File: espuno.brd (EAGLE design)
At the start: 68.6 x 53.3 mm, 62 parts, among them J1 ARDUINO_R3_SHIELD, T1 FDN340P, U1 ADS1115IDGST, U2 NCP1117ST50T3G, U3 LP2985-33DBVR, U4 FT232R, U5 LMV358IDGKR, U6 MCP73831, U7 TPS61200, X1 POWERSUPPLY_DC21MMX

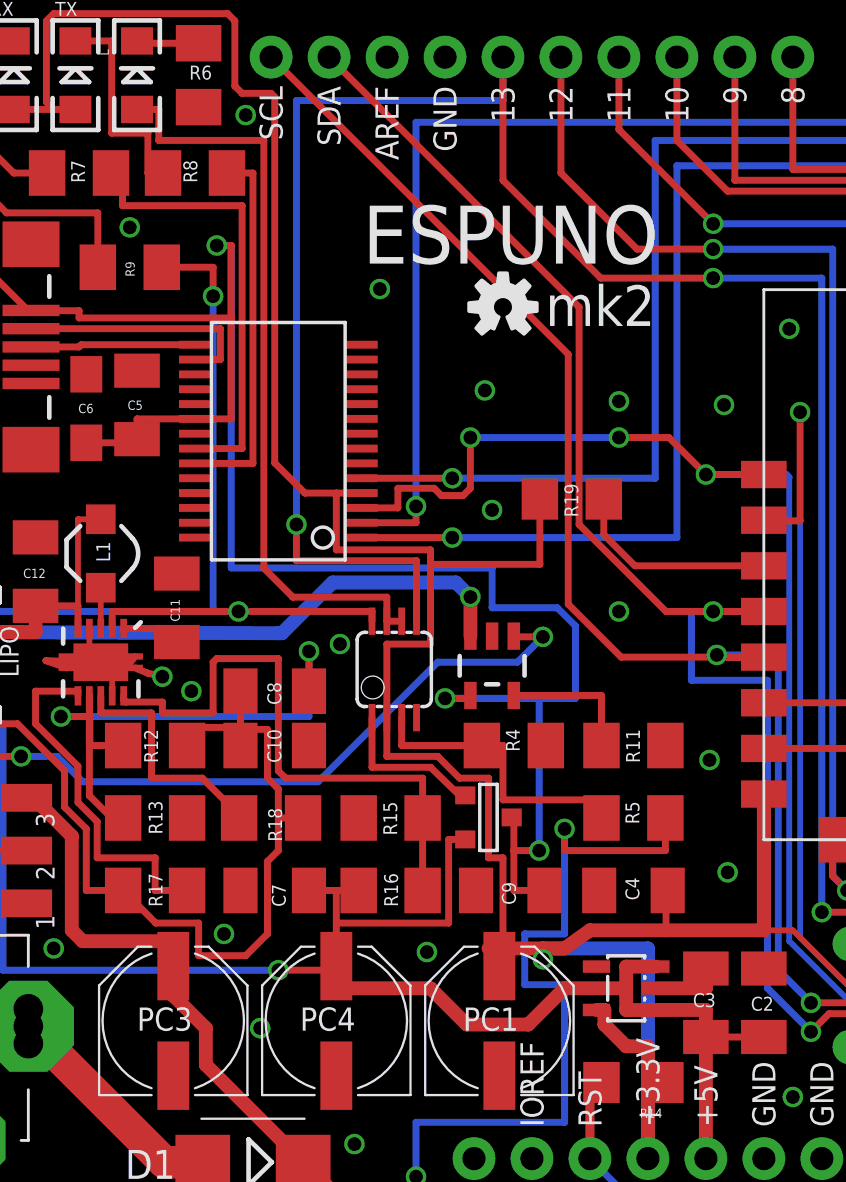
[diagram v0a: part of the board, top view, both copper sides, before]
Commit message: Fix bug with TX/RX switched, renumber PC1,PC3,PC4 to be PC1-3 in order of decreasing voltage rail.
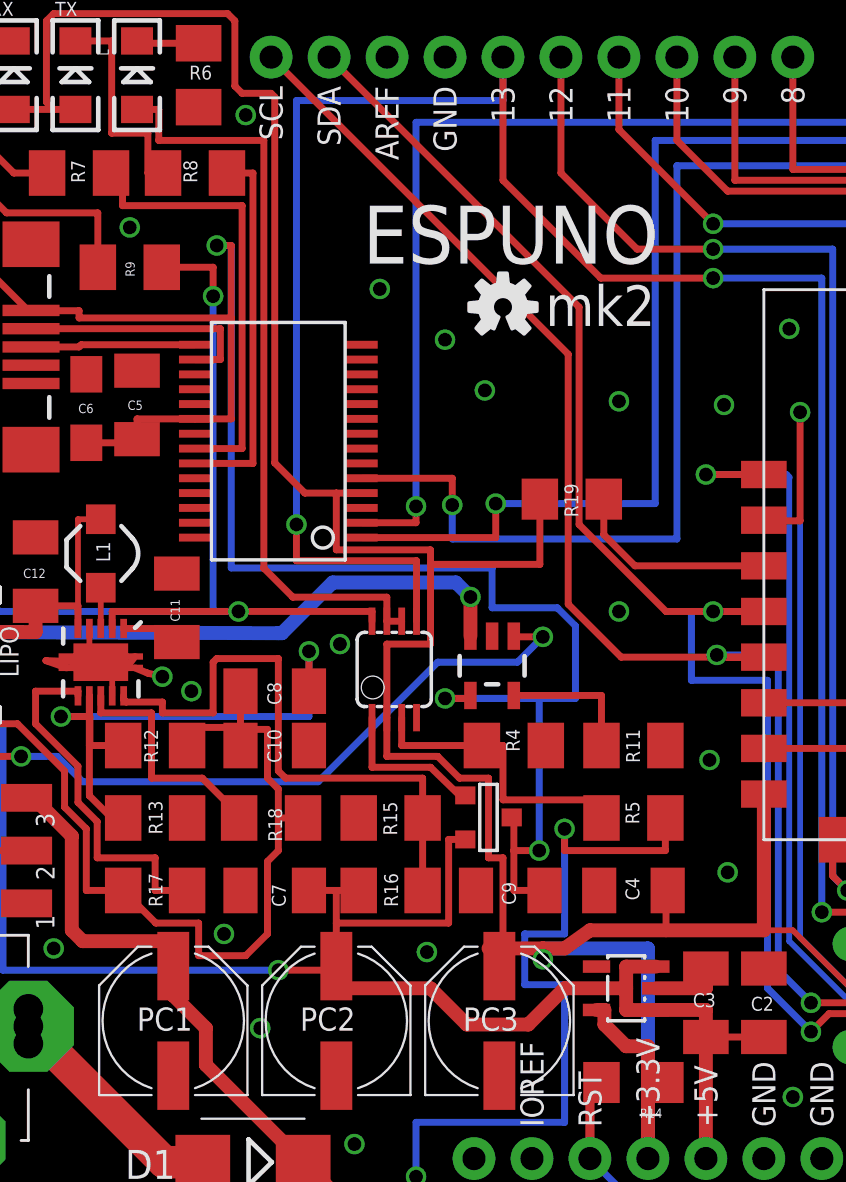
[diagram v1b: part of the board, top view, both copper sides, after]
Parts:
- moved PC1 14.3 mm to (14.8, 8.57)
- moved PC3 14.3 mm to (29.1, 8.57)
- renumbered PC4 to PC2
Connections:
- net 3.3V: now also PC3.+; no longer PC1.+
- net RESET: no longer U4.3
- net RX: now also U4.1; no longer U4.5
- net TX: now also U4.5; no longer U4.1
- net VIN: now also PC1.+; no longer PC3.+
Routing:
- net RESET: track 126.2 -> 107.1 mm, vias 3 -> 1
- net TX: track 79.4 -> 82.1 mm
- net RX: track 85.9 -> 88.5 mm
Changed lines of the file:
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@@
 <?xml version="1.0" encoding="utf-8"?>
 <!DOCTYPE eagle SYSTEM "eagle.dtd">
-<eagle version="7.2.0">
+<eagle version="7.4.0">
 <drawing>
 <settings>
@@
 <grid distance="0.00625" unitdist="inch" unit="inch" style="lines" multiple="1" display="no" altdistance="0.00625" altunitdist="inch" altunit="inch"/>
 <layers>
-<layer number="1" name="Top" color="4" fill="1" visible="no" active="yes"/>
-<layer number="16" name="Bottom" color="1" fill="1" visible="no" active="yes"/>
+<layer number="1" name="Top" color="4" fill="1" visible="yes" active="yes"/>
+<layer number="16" name="Bottom" color="1" fill="1" visible="yes" active="yes"/>
 <layer number="17" name="Pads" color="2" fill="1" visible="yes" active="yes"/>
 <layer number="18" name="Vias" color="2" fill="1" visible="yes" active="yes"/>
@@
 <element name="JP1" library="SparkFun-Connectors" package="USB-MINIB-NOSTOP" value="USB-SMD-NS" x="6.0325" y="38.1" smashed="yes"/>
 <element name="J1" library="SparkFun-Boards" package="UNO_R3_SHIELD" value="ARDUINO_R3_SHIELD" x="8.89" y="53.34" smashed="yes" rot="R270"/>
-<element name="PC3" library="rcl" package="PANASONIC_D" value="47u" x="14.76375" y="8.5725" smashed="yes" rot="R90">
+<element name="PC1" library="rcl" package="PANASONIC_D" value="47u" x="14.76375" y="8.5725" smashed="yes" rot="R90">
 <attribute name="NAME" x="13.1725" y="8.14375" size="1.016" layer="25"/>
 </element>
-<element name="PC4" library="rcl" package="PANASONIC_D" value="47u" x="21.9075" y="8.5725" smashed="yes" rot="R90">
+<element name="PC2" library="rcl" package="PANASONIC_D" value="47u" x="21.9075" y="8.5725" smashed="yes" rot="R90">
 <attribute name="NAME" x="20.31625" y="8.14375" size="1.016" layer="25"/>
 </element>
-<element name="PC1" library="rcl" package="PANASONIC_D" value="47u" x="29.05125" y="8.5725" smashed="yes" rot="R90">
+<element name="PC3" library="rcl" package="PANASONIC_D" value="47u" x="29.05125" y="8.5725" smashed="yes" rot="R90">
 <attribute name="NAME" x="27.46" y="8.14375" size="1.016" layer="25"/>
 </element>
@@
 <signal name="RX">
 <contactref element="MDL1" pad="15"/>
-<contactref element="U4" pad="5"/>
 <contactref element="J1" pad="RX"/>
 <wire x1="56.84" y1="30.51" x2="61.43625" y2="30.51" width="0.3048" layer="1"/>
@@
 <wire x1="61.43625" y1="48.895" x2="63.5" y2="48.895" width="0.3048" layer="1"/>
 <wire x1="63.5" y1="48.895" x2="63.5" y2="50.8" width="0.3048" layer="1"/>
-<wire x1="23.0235" y1="32.3475" x2="26.9875" y2="32.3475" width="0.3048" layer="1"/>
-<via x="26.9875" y="32.3475" extent="1-16" drill="0.6"/>
-<wire x1="26.9875" y1="32.3475" x2="35.8775" y2="32.3475" width="0.3048" layer="16"/>
-<wire x1="35.8775" y1="32.3475" x2="35.8775" y2="47.14875" width="0.3048" layer="16"/>
+<via x="28.8925" y="31.23625" extent="1-16" drill="0.6"/>
+<wire x1="28.8925" y1="31.23625" x2="35.8775" y2="31.23625" width="0.3048" layer="16"/>
+<wire x1="35.8775" y1="31.23625" x2="35.8775" y2="47.14875" width="0.3048" layer="16"/>
 <wire x1="35.8775" y1="47.14875" x2="63.5" y2="47.14875" width="0.3048" layer="16"/>
 <wire x1="63.5" y1="47.14875" x2="63.5" y2="50.8" width="0.3048" layer="16"/>
+<contactref element="U4" pad="1"/>
+<wire x1="23.0235" y1="29.7475" x2="28.8925" y2="29.7475" width="0.3048" layer="1"/>
+<wire x1="28.8925" y1="29.7475" x2="28.8925" y2="31.23625" width="0.3048" layer="1"/>
 </signal>
 <signal name="TX">
 <contactref element="MDL1" pad="16"/>
-<contactref element="U4" pad="1"/>
 <contactref element="J1" pad="TX"/>
 <wire x1="56.84" y1="32.51" x2="58.26125" y2="32.51" width="0.3048" layer="1"/>
@@
 <wire x1="60.96" y1="31.115" x2="60.96" y2="46.0375" width="0.3048" layer="1"/>
 <wire x1="60.96" y1="46.0375" x2="60.96" y2="50.8" width="0.3048" layer="1"/>
-<wire x1="23.0235" y1="29.7475" x2="26.9875" y2="29.7475" width="0.3048" layer="1"/>
-<via x="26.9875" y="29.7475" extent="1-16" drill="0.6"/>
-<wire x1="26.9875" y1="29.7475" x2="36.83" y2="29.7475" width="0.3048" layer="16"/>
-<wire x1="36.83" y1="29.7475" x2="36.83" y2="46.0375" width="0.3048" layer="16"/>
+<via x="26.9875" y="31.17625" extent="1-16" drill="0.6"/>
+<wire x1="26.9875" y1="31.17625" x2="26.9875" y2="29.68625" width="0.3048" layer="16"/>
+<wire x1="26.9875" y1="29.68625" x2="36.83" y2="29.68625" width="0.3048" layer="16"/>
+<wire x1="36.83" y1="29.68625" x2="36.83" y2="46.0375" width="0.3048" layer="16"/>
 <wire x1="36.83" y1="46.0375" x2="59.69" y2="46.0375" width="0.3048" layer="16"/>
 <via x="59.69" y="46.0375" extent="1-16" drill="0.6"/>
 <wire x1="59.69" y1="46.0375" x2="60.96" y2="46.0375" width="0.3048" layer="1"/>
+<contactref element="U4" pad="5"/>
+<wire x1="23.0235" y1="32.3475" x2="26.9875" y2="32.3475" width="0.3048" layer="1"/>
+<wire x1="26.9875" y1="32.3475" x2="26.9875" y2="31.17625" width="0.3048" layer="1"/>
 </signal>
 <signal name="2/GPIO5">
@@
 <wire x1="67.78625" y1="7.42315" x2="51.66995" y2="7.42315" width="0.3048" layer="16"/>
 <contactref element="R14" pad="2"/>
-<contactref element="U4" pad="3"/>
 <wire x1="33.525" y1="5.87375" x2="33.02" y2="6.0325" width="0.4064" layer="1"/>
 <wire x1="33.02" y1="6.0325" x2="33.02" y2="2.54" width="0.4064" layer="1"/>
-<wire x1="23.0235" y1="31.0475" x2="24.60625" y2="31.0475" width="0.3048" layer="1"/>
-<wire x1="24.60625" y1="31.0475" x2="24.60625" y2="31.90875" width="0.3048" layer="1"/>
-<wire x1="24.60625" y1="31.90875" x2="26.19375" y2="31.90875" width="0.3048" layer="1"/>
-<wire x1="26.19375" y1="31.90875" x2="26.51125" y2="31.59125" width="0.3048" layer="1"/>
-<wire x1="26.51125" y1="31.59125" x2="27.46375" y2="31.59125" width="0.3048" layer="1"/>
-<wire x1="27.46375" y1="31.59125" x2="27.78125" y2="31.90875" width="0.3048" layer="1"/>
-<wire x1="27.78125" y1="31.90875" x2="27.78125" y2="34.13125" width="0.3048" layer="1"/>
-<via x="27.78125" y="34.13125" extent="1-16" drill="0.6"/>
-<wire x1="27.78125" y1="34.13125" x2="34.29" y2="34.13125" width="0.3048" layer="16"/>
-<via x="34.29" y="34.13125" extent="1-16" drill="0.6"/>
-<wire x1="34.29" y1="34.13125" x2="36.47875" y2="34.13125" width="0.3048" layer="1"/>
-<wire x1="36.47875" y1="34.13125" x2="38.1" y2="32.51" width="0.3048" layer="1"/>
 </signal>
 <signal name="3.3V">
@@
 <wire x1="34.6075" y1="7.46125" x2="35.56" y2="7.46125" width="0.6096" layer="1"/>
 <wire x1="35.56" y1="7.46125" x2="35.56" y2="6.19125" width="0.6096" layer="1"/>
-<contactref element="PC1" pad="+"/>
+<contactref element="PC3" pad="+"/>
 <wire x1="35.56" y1="6.19125" x2="35.56" y2="2.54" width="0.6096" layer="1"/>
 <wire x1="29.05125" y1="10.9725" x2="29.05125" y2="11.7475" width="0.6096" layer="1"/>
@@
 <contactref element="J1" pad="GND@2"/>
 <contactref element="J1" pad="GND@0"/>
-<contactref element="PC3" pad="-"/>
-<contactref element="PC4" pad="-"/>
+<contactref element="PC1" pad="-"/>
+<contactref element="PC2" pad="-"/>
 <wire x1="13.08875" y1="24.53875" x2="12.72375" y2="24.0625" width="0.3048" layer="1"/>
 <wire x1="12.72375" y1="24.0625" x2="12.08875" y2="23.97125" width="0.3048" layer="1"/>
@@
 <wire x1="9.18375" y1="24.35625" x2="11.08875" y2="24.28875" width="0.3048" layer="1"/>
 <via x="2.69875" y="23.495" extent="1-16" drill="0.6"/>
-<via x="28.73375" y="30.95625" extent="1-16" drill="0.6"/>
+<via x="26.67" y="38.4175" extent="1-16" drill="0.6"/>
 <via x="17.93875" y="48.26" extent="1-16" drill="0.6"/>
 <via x="14.2875" y="23.65375" extent="1-16" drill="0.6"/>
@@
 <wire x1="35.9075" y1="10.00125" x2="38.1" y2="10.00125" width="0.6096" layer="1"/>
 <wire x1="38.1" y1="10.00125" x2="38.1" y2="10.86625" width="0.6096" layer="1"/>
-<contactref element="PC1" pad="-"/>
+<contactref element="PC3" pad="-"/>
 <via x="25.87625" y="11.58875" extent="1-16" drill="0.6"/>
 <wire x1="20.70875" y1="20.6375" x2="20.70875" y2="21.43125" width="0.3048" layer="1"/>
@@
 <wire x1="6.50875" y1="27.14625" x2="7.14375" y2="26.51125" width="0.3048" layer="16"/>
 <wire x1="7.14375" y1="26.51125" x2="17.62125" y2="26.51125" width="0.3048" layer="16"/>
-<contactref element="PC4" pad="+"/>
+<contactref element="PC2" pad="+"/>
 <wire x1="21.9075" y1="10.795" x2="19.3675" y2="10.795" width="0.3048" layer="1"/>
 <via x="19.3675" y="10.795" extent="1-16" drill="0.6"/>
@@
 <contactref element="R5" pad="2"/>
 <contactref element="J1" pad="VIN"/>
-<contactref element="PC3" pad="+"/>
+<contactref element="PC1" pad="+"/>
 <wire x1="20.45625" y1="2.38125" x2="22.04375" y2="0.79375" width="0.6096" layer="1"/>
 <wire x1="22.04375" y1="0.79375" x2="25.24125" y2="0.79375" width="0.6096" layer="1"/>

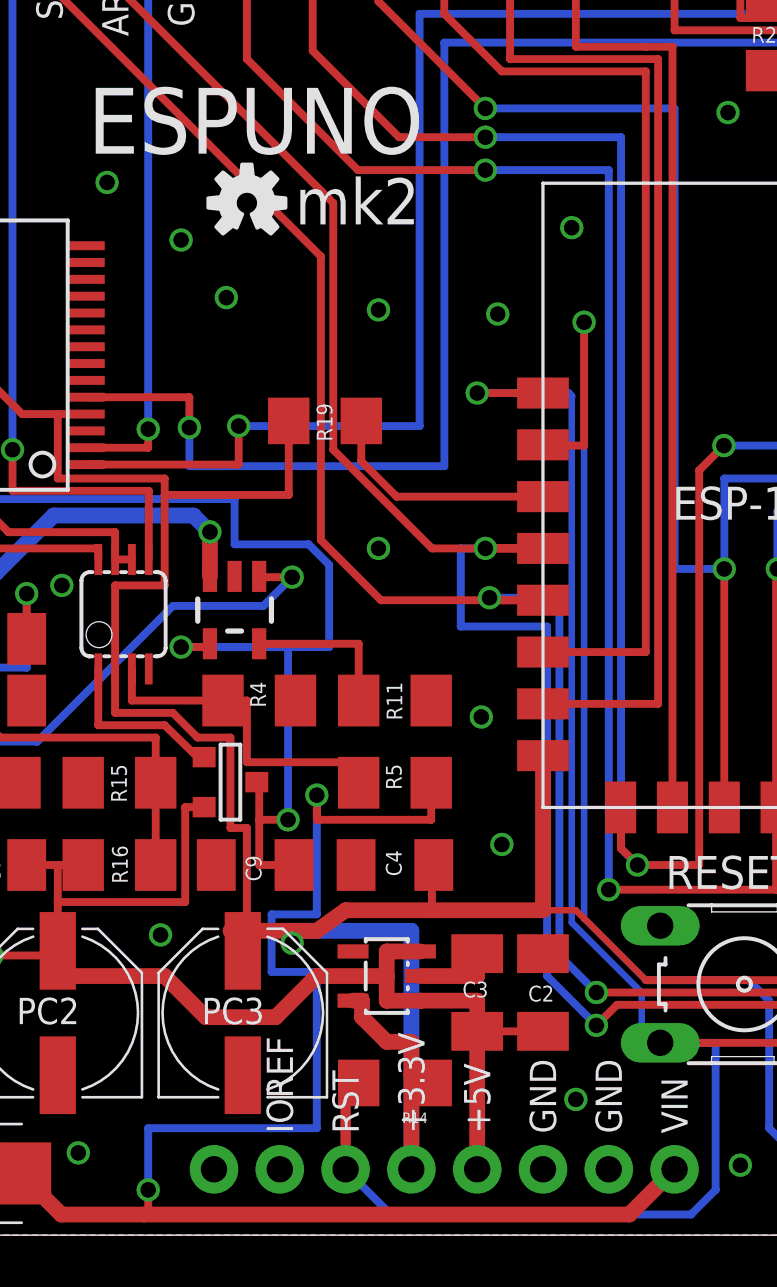
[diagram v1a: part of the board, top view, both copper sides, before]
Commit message: Change puny 3.3v regulator for a 800mA-1A regulator. Rearrangements to make space, remove redundent capacitor
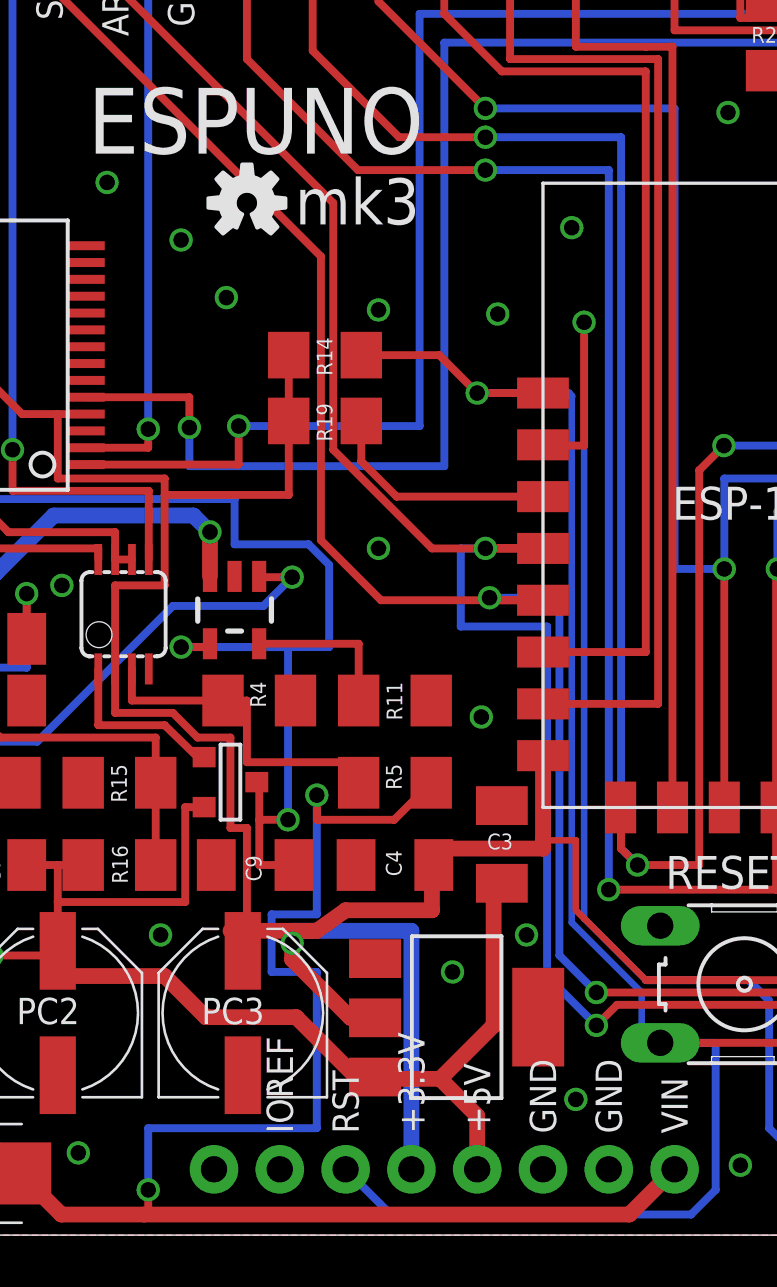
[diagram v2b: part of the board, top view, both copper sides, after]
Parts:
- removed C2: 0.1uf, rcl:C1206K
- removed U3: LP2985-33DBVR, SmartPrj:SOT23-DBV
- added IC1: REG1117, burr-brown:SOT223
- moved R14 28.2 mm to (32.2, 34.0), turned to 0 degrees
- moved C3 5.79 mm to (39.1, 15.1)
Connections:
- net 3.3V: now also IC1.2; no longer U3.5
- net 5V: now also IC1.3; no longer C2.2, U3.1, U3.3
- net GND: now also IC1.1; no longer C2.1, U3.2
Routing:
- net GND: track 13.5 -> 10.4 mm, vias 34 -> 35
- net RESET: track 107.1 -> 108.2 mm
- net 3.3V: track 201.5 -> 202.3 mm
- net VIN: track 83.3 -> 82.4 mm
- net 5V: track 138.0 -> 137.4 mm
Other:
- board text added: "mk3"
- board text removed: "mk2"
